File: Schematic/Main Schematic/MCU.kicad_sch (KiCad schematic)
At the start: 10 parts, among them J7 Conn_01x02_Pin, U4 M24C16-RMN6TP

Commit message: No change
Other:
- note removed: "TO-DO - Female headers should be inside MCU - UART Tx - Rx and Rx to Tx - Add Pull-up Resistors to SCL & SDA - Vcc connects to power not GND"
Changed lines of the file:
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@@
     (stroke (width 0) (type default))
-  )
-  (text "TO-DO\n- Female headers should be inside MCU\n- UART Tx - Rx and Rx to Tx\n- Add Pull-up Resistors to SCL & SDA\n- Vcc connects to power not GND\n"
-    (at 31.75 127 0)
-    (effects (font (size 1.27 1.27)) (justify left bottom))
   )
   (text "TEAM 26\nSIVUYILE NOSE\nMODULE INTERFACES WITH SENSOR AND POWER MODULES\nUCT\n"

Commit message: I've added the local footprints and gerber files into the repo
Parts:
- C8, C?: footprint A_New_folder:C1206 -> Local_Footprints:C1206
- U4: footprint A_New_folder:SOIC-8_L5.0-W4.0-P1.27-LS6.0-BL -> Local_Footprints:SOIC-8_L5.0-W4.0-P1.27-LS6.0-BL
- U?: footprint A_New_folder:SOP-16_L10.0-W3.9-P1.27-LS6.0-BL -> Local_Footprints:SOP-16_L10.0-W3.9-P1.27-LS6.0-BL
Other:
- note added: "TO-DO - Female headers should be inside MCU - UART Tx - Rx and Rx to Tx - Add Pull-up Resistors to SCL & SDA - Vcc connects to power not GND"
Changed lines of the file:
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@@
     (stroke (width 0) (type default))
+  )
+  (text "TO-DO\n- Female headers should be inside MCU\n- UART Tx - Rx and Rx to Tx\n- Add Pull-up Resistors to SCL & SDA\n- Vcc connects to power not GND\n"
+    (at 31.75 127 0)
+    (effects (font (size 1.27 1.27)) (justify left bottom))
   )
   (text "TEAM 26\nSIVUYILE NOSE\nMODULE INTERFACES WITH SENSOR AND POWER MODULES\nUCT\n"
@@
       (effects (font (size 1.27 1.27)))
     )
-    (property "Footprint" "A_New_folder:C1206" (at 107.95 40.9448 0)
+    (property "Footprint" "Local_Footprints:C1206" (at 107.95 40.9448 0)
       (effects (font (size 1.27 1.27)) hide)
     )
@@
       (effects (font (size 1.27 1.27)))
     )
-    (property "Footprint" "A_New_folder:SOP-16_L10.0-W3.9-P1.27-LS6.0-BL" (at 78.74 59.69 0)
+    (property "Footprint" "Local_Footprints:SOP-16_L10.0-W3.9-P1.27-LS6.0-BL" (at 78.74 59.69 0)
       (effects (font (size 1.27 1.27)) (justify bottom) hide)
     )
@@
       (effects (font (size 1.27 1.27)) (justify left))
     )
-    (property "Footprint" "A_New_folder:C1206" (at 251.1552 67.31 0)
+    (property "Footprint" "Local_Footprints:C1206" (at 251.1552 67.31 0)
       (effects (font (size 1.27 1.27)) hide)
     )
@@
       (effects (font (size 1.27 1.27)))
     )
-    (property "Footprint" "A_New_folder:SOIC-8_L5.0-W4.0-P1.27-LS6.0-BL" (at 215.9 64.77 0)
+    (property "Footprint" "Local_Footprints:SOIC-8_L5.0-W4.0-P1.27-LS6.0-BL" (at 215.9 64.77 0)
       (effects (font (size 1.27 1.27)) (justify left bottom) hide)
     )

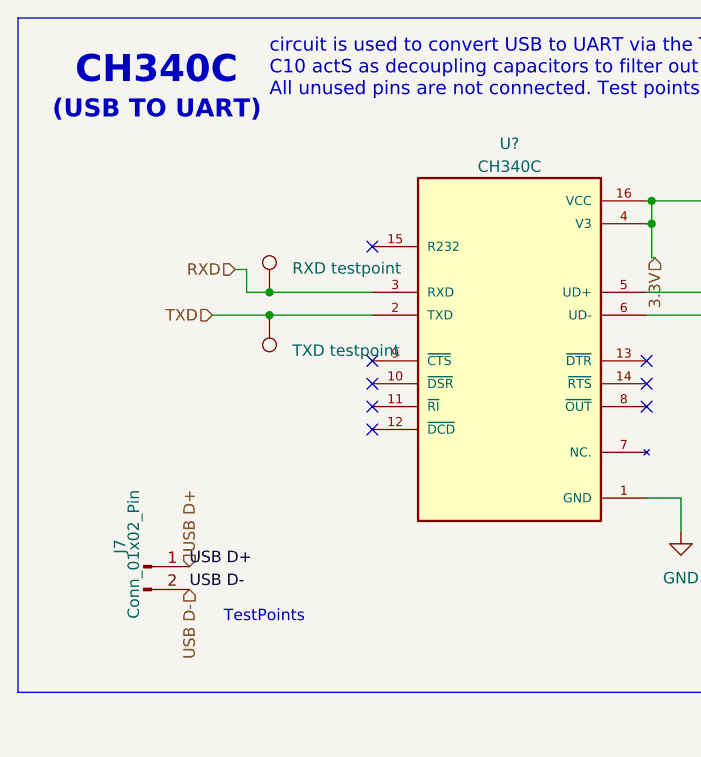
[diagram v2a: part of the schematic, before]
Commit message: LED added for visuals
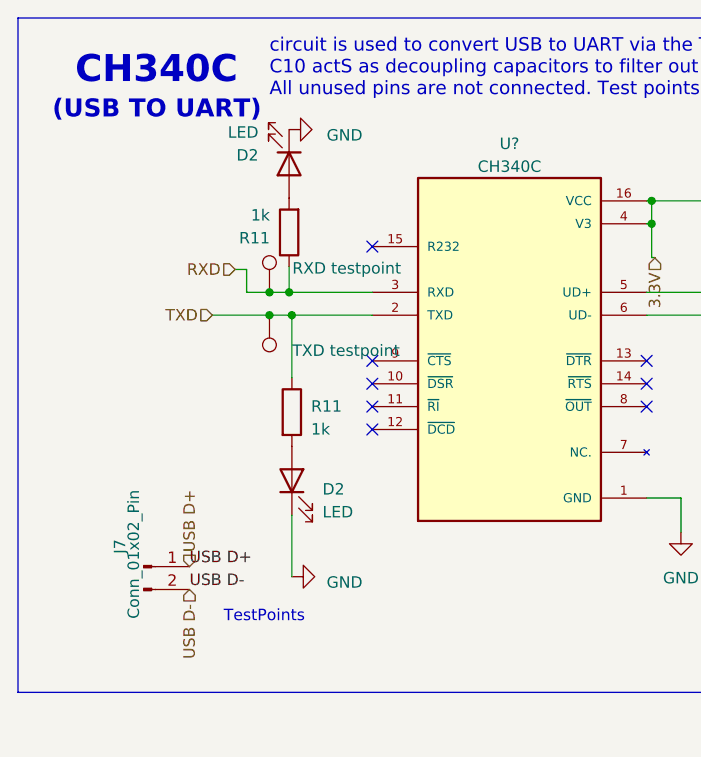
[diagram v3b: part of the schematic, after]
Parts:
- added D2 (x2): LED, symbol Device:LED
- added R11 (x2): 1k, symbol Device:R
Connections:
- net GND: now also D2.1 (K), D2.1 (K)
- net RXD: now also R11.1
- net TXD: now also R11.1
- new net: D2.2 (A), R11.2 (x2)
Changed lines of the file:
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@@
   (junction (at 191.77 57.15) (diameter 0) (color 0 0 0 0)
   )
+  (junction (at 54.5592 54.61) (diameter 0) (color 0 0 0 0)
+  )
   (junction (at 186.69 67.31) (diameter 0) (color 0 0 0 0)
   )
@@
   )
   (junction (at 52.07 52.07) (diameter 0) (color 0 0 0 0)
+  )
+  (junction (at 54.2544 52.07) (diameter 0) (color 0 0 0 0)
   )
   (junction (at 241.3 59.69) (diameter 0) (color 0 0 0 0)
@@
     (stroke (width 0) (type default))
   )
-  (wire (pts (xy 52.07 54.61) (xy 63.5 54.61))
+  (wire (pts (xy 52.07 54.61) (xy 54.5592 54.61))
     (stroke (width 0) (type default))
   )
@@
     (stroke (width 0) (type default))
   )
+  (wire (pts (xy 54.5592 54.61) (xy 54.5592 61.5696))
+    (stroke (width 0) (type default))
+  )
   (wire (pts (xy 194.31 69.85) (xy 200.66 69.85))
     (stroke (width 0) (type default))
@@
     (stroke (width 0) (type default))
   )
+  (wire (pts (xy 54.5592 54.61) (xy 63.5 54.61))
+    (stroke (width 0) (type default))
+  )
+  (wire (pts (xy 54.2544 49.2252) (xy 54.2544 52.07))
+    (stroke (width 0) (type default))
+  )
+  (wire (pts (xy 54.5592 76.8096) (xy 54.5592 83.6676))
+    (stroke (width 0) (type default))
+  )
   (wire (pts (xy 48.26 49.53) (xy 49.53 49.53))
     (stroke (width 0) (type default))
@@
     (stroke (width 0) (type default))
   )
+  (wire (pts (xy 54.2544 52.07) (xy 63.5 52.07))
+    (stroke (width 0) (type default))
+  )
   (wire (pts (xy 200.66 62.23) (xy 186.69 62.23))
     (stroke (width 0) (type default))
@@
     (stroke (width 0) (type default))
   )
-  (wire (pts (xy 52.07 52.07) (xy 63.5 52.07))
+  (wire (pts (xy 52.07 52.07) (xy 54.2544 52.07))
     (stroke (width 0) (type default))
   )
@@
     )
   )
+  (symbol (lib_id "Device:R") (at 54.2544 45.4152 180) (unit 1)
+    (in_bom yes) (on_board yes) (dnp no) (fields_autoplaced)
+    (property "Reference" "R11" (at 52.1208 46.0502 0)
+      (effects (font (size 1.27 1.27)) (justify left))
+    )
+    (property "Value" "1k" (at 52.1208 43.5102 0)
+      (effects (font (size 1.27 1.27)) (justify left))
+    )
+    (property "Footprint" "" (at 56.0324 45.4152 90)
+      (effects (font (size 1.27 1.27)) hide)
+    )
+    (property "Datasheet" "~" (at 54.2544 45.4152 0)
+      (effects (font (size 1.27 1.27)) hide)
+    )
+    (pin "1")
+    (pin "2")
+    (instances
+      (project "Main Schematic"
+        (path "/81c41bad-bb43-41af-b405-18d135a809b1/297def35-fe1a-4185-9e34-6248c2c818f7"
+          (reference "R11") (unit 1)
+        )
+        (path "/81c41bad-bb43-41af-b405-18d135a809b1/ae15d31d-f7b4-4051-b9d0-3a01939afe0e"
+          (reference "R15") (unit 1)
+        )
+      )
+    )
+  )
   (symbol (lib_id "power:GND") (at 186.69 68.58 0) (unit 1)
     (in_bom yes) (on_board yes) (dnp no) (fields_autoplaced)
@@
     )
   )
+  (symbol (lib_id "power:GND") (at 54.2544 33.9852 90) (unit 1)
+    (in_bom yes) (on_board yes) (dnp no) (fields_autoplaced)
+    (property "Reference" "#PWR024" (at 60.6044 33.9852 0)
+      (effects (font (size 1.27 1.27)) hide)
+    )
+    (property "Value" "GND" (at 58.42 34.6202 90)
+      (effects (font (size 1.27 1.27)) (justify right))
+    )
+    (property "Footprint" "" (at 54.2544 33.9852 0)
+      (effects (font (size 1.27 1.27)) hide)
+    )
+    (property "Datasheet" "" (at 54.2544 33.9852 0)
+      (effects (font (size 1.27 1.27)) hide)
+    )
+    (pin "1")
+    (instances
+      (project "Main Schematic"
+        (path "/81c41bad-bb43-41af-b405-18d135a809b1/ae15d31d-f7b4-4051-b9d0-3a01939afe0e"
+          (reference "#PWR024") (unit 1)
+        )
+      )
+    )
+  )
+  (symbol (lib_id "power:GND") (at 54.5592 83.6676 90) (unit 1)
+    (in_bom yes) (on_board yes) (dnp no) (fields_autoplaced)
+    (property "Reference" "#PWR07" (at 60.9092 83.6676 0)
+      (effects (font (size 1.27 1.27)) hide)
+    )
+    (property "Value" "GND" (at 58.42 84.3026 90)
+      (effects (font (size 1.27 1.27)) (justify right))
+    )
+    (property "Footprint" "" (at 54.5592 83.6676 0)
+      (effects (font (size 1.27 1.27)) hide)
+    )
+    (property "Datasheet" "" (at 54.5592 83.6676 0)
+      (effects (font (size 1.27 1.27)) hide)
+    )
+    (pin "1")
+    (instances
+      (project "Main Schematic"
+        (path "/81c41bad-bb43-41af-b405-18d135a809b1/ae15d31d-f7b4-4051-b9d0-3a01939afe0e"
+          (reference "#PWR07") (unit 1)
+        )
+      )
+    )
+  )
   (symbol (lib_id "Connector:TestPoint") (at 52.07 54.61 180) (unit 1)
     (in_bom yes) (on_board yes) (dnp no) (fields_autoplaced)
@@
     )
   )
+  (symbol (lib_id "Device:LED") (at 54.2544 37.7952 270) (unit 1)
+    (in_bom yes) (on_board yes) (dnp no) (fields_autoplaced)
+    (property "Reference" "D2" (at 50.8508 36.8427 90)
+      (effects (font (size 1.27 1.27)) (justify right))
+    )
+    (property "Value" "LED" (at 50.8508 34.3027 90)
+      (effects (font (size 1.27 1.27)) (justify right))
+    )
+    (property "Footprint" "" (at 54.2544 37.7952 0)
+      (effects (font (size 1.27 1.27)) hide)
+    )
+    (property "Datasheet" "~" (at 54.2544 37.7952 0)
+      (effects (font (size 1.27 1.27)) hide)
+    )
+    (pin "1")
+    (pin "2")
+    (instances
+      (project "Main Schematic"
+        (path "/81c41bad-bb43-41af-b405-18d135a809b1/297def35-fe1a-4185-9e34-6248c2c818f7"
+          (reference "D2") (unit 1)
+        )
+        (path "/81c41bad-bb43-41af-b405-18d135a809b1/ae15d31d-f7b4-4051-b9d0-3a01939afe0e"
+          (reference "D6") (unit 1)
+        )
+      )
+    )
+  )
+  (symbol (lib_id "Device:LED") (at 54.5592 72.9996 90) (unit 1)
+    (in_bom yes) (on_board yes) (dnp no) (fields_autoplaced)
+    (property "Reference" "D2" (at 57.9628 73.9521 90)
+      (effects (font (size 1.27 1.27)) (justify right))
+    )
+    (property "Value" "LED" (at 57.9628 76.4921 90)
+      (effects (font (size 1.27 1.27)) (justify right))
+    )
+    (property "Footprint" "" (at 54.5592 72.9996 0)
+      (effects (font (size 1.27 1.27)) hide)
+    )
+    (property "Datasheet" "~" (at 54.5592 72.9996 0)
+      (effects (font (size 1.27 1.27)) hide)
+    )
+    (pin "1")
+    (pin "2")
+    (instances
+      (project "Main Schematic"
+        (path "/81c41bad-bb43-41af-b405-18d135a809b1/297def35-fe1a-4185-9e34-6248c2c818f7"
+          (reference "D2") (unit 1)
+        )
+        (path "/81c41bad-bb43-41af-b405-18d135a809b1/ae15d31d-f7b4-4051-b9d0-3a01939afe0e"
+          (reference "D5") (unit 1)
+        )
+      )
+    )
+  )
   (symbol (lib_id "Connector:TestPoint") (at 234.95 64.77 270) (unit 1)
     (in_bom yes) (on_board yes) (dnp no) (fields_autoplaced)
@@
         )
       )
+    )
+  )
+  (symbol (lib_id "Device:R") (at 54.5592 65.3796 0) (unit 1)
+    (in_bom yes) (on_board yes) (dnp no) (fields_autoplaced)
+    (property "Reference" "R11" (at 56.6928 64.7446 0)
+      (effects (font (size 1.27 1.27)) (justify left))
+    )
+    (property "Value" "1k" (at 56.6928 67.2846 0)
+      (effects (font (size 1.27 1.27)) (justify left))
+    )
+    (property "Footprint" "" (at 52.7812 65.3796 90)
+      (effects (font (size 1.27 1.27)) hide)
+    )
+    (property "Datasheet" "~" (at 54.5592 65.3796 0)
+      (effects (font (size 1.27 1.27)) hide)
+    )
+    (pin "1")
+    (pin "2")
+    (instances
+      (project "Main Schematic"
+        (path "/81c41bad-bb43-41af-b405-18d135a809b1/297def35-fe1a-4185-9e34-6248c2c818f7"
+          (reference "R11") (unit 1)
+        )
+        (path "/81c41bad-bb43-41af-b405-18d135a809b1/ae15d31d-f7b4-4051-b9d0-3a01939afe0e"
+          (reference "R14") (unit 1)
+        )
+      )

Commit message: Added more led for visual indications, also changed debugger pins to 9 pins for 3.3v pin
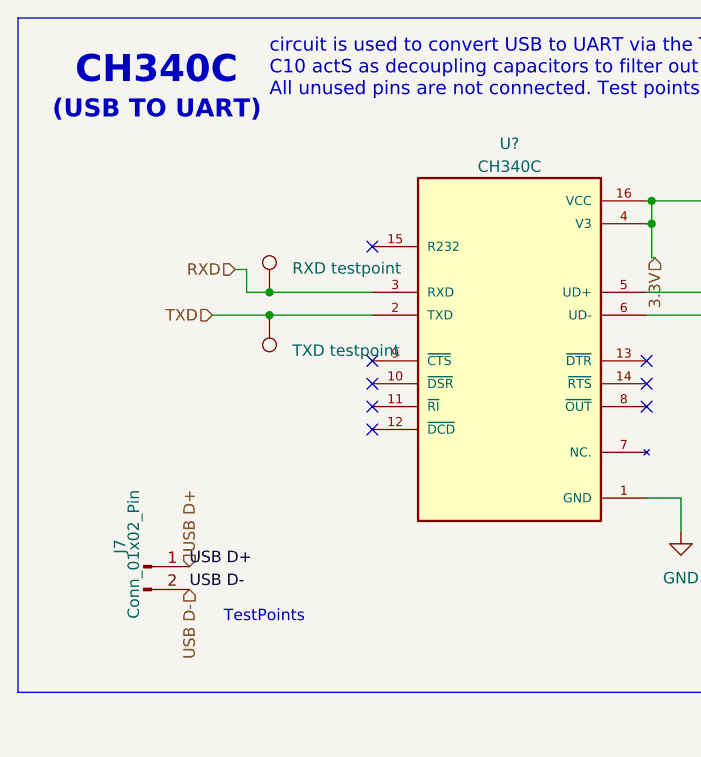
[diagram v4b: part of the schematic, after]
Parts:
- removed D2 (x2): LED, symbol Device:LED
- removed R11 (x2): 1k, symbol Device:R
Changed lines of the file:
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@@
   (junction (at 191.77 57.15) (diameter 0) (color 0 0 0 0)
   )
-  (junction (at 54.5592 54.61) (diameter 0) (color 0 0 0 0)
-  )
   (junction (at 186.69 67.31) (diameter 0) (color 0 0 0 0)
   )
@@
   )
   (junction (at 52.07 52.07) (diameter 0) (color 0 0 0 0)
-  )
-  (junction (at 54.2544 52.07) (diameter 0) (color 0 0 0 0)
   )
   (junction (at 241.3 59.69) (diameter 0) (color 0 0 0 0)
@@
     (stroke (width 0) (type default))
   )
-  (wire (pts (xy 52.07 54.61) (xy 54.5592 54.61))
-    (stroke (width 0) (type default))
-  )
   (wire (pts (xy 94.5388 41.91) (xy 100.33 41.91))
     (stroke (width 0) (type default))
@@
     (stroke (width 0) (type default))
   )
-  (wire (pts (xy 54.5592 54.61) (xy 54.5592 61.5696))
-    (stroke (width 0) (type default))
-  )
   (wire (pts (xy 194.31 69.85) (xy 200.66 69.85))
     (stroke (width 0) (type default))
@@
     (stroke (width 0) (type default))
   )
-  (wire (pts (xy 54.5592 54.61) (xy 63.5 54.61))
-    (stroke (width 0) (type default))
-  )
-  (wire (pts (xy 54.2544 49.2252) (xy 54.2544 52.07))
-    (stroke (width 0) (type default))
-  )
-  (wire (pts (xy 54.5592 76.8096) (xy 54.5592 83.6676))
+  (wire (pts (xy 52.07 54.61) (xy 63.5 54.61))
     (stroke (width 0) (type default))
   )
@@
     (stroke (width 0) (type default))
   )
-  (wire (pts (xy 54.2544 52.07) (xy 63.5 52.07))
-    (stroke (width 0) (type default))
-  )
   (wire (pts (xy 200.66 62.23) (xy 186.69 62.23))
     (stroke (width 0) (type default))
@@
     (stroke (width 0) (type default))
   )
-  (wire (pts (xy 52.07 52.07) (xy 54.2544 52.07))
+  (wire (pts (xy 52.07 52.07) (xy 63.5 52.07))
     (stroke (width 0) (type default))
   )
@@
     )
   )
-  (symbol (lib_id "Device:R") (at 54.2544 45.4152 180) (unit 1)
-    (in_bom yes) (on_board yes) (dnp no) (fields_autoplaced)
-    (property "Reference" "R11" (at 52.1208 46.0502 0)
-      (effects (font (size 1.27 1.27)) (justify left))
-    )
-    (property "Value" "1k" (at 52.1208 43.5102 0)
-      (effects (font (size 1.27 1.27)) (justify left))
-    )
-    (property "Footprint" "" (at 56.0324 45.4152 90)
-      (effects (font (size 1.27 1.27)) hide)
-    )
-    (property "Datasheet" "~" (at 54.2544 45.4152 0)
-      (effects (font (size 1.27 1.27)) hide)
-    )
-    (pin "1")
-    (pin "2")
-    (instances
-      (project "Main Schematic"
-        (path "/81c41bad-bb43-41af-b405-18d135a809b1/297def35-fe1a-4185-9e34-6248c2c818f7"
-          (reference "R11") (unit 1)
-        )
-        (path "/81c41bad-bb43-41af-b405-18d135a809b1/ae15d31d-f7b4-4051-b9d0-3a01939afe0e"
-          (reference "R15") (unit 1)
-        )
-      )
-    )
-  )
   (symbol (lib_id "power:GND") (at 186.69 68.58 0) (unit 1)
     (in_bom yes) (on_board yes) (dnp no) (fields_autoplaced)
@@
     )
   )
-  (symbol (lib_id "power:GND") (at 54.2544 33.9852 90) (unit 1)
-    (in_bom yes) (on_board yes) (dnp no) (fields_autoplaced)
-    (property "Reference" "#PWR024" (at 60.6044 33.9852 0)
-      (effects (font (size 1.27 1.27)) hide)
-    )
-    (property "Value" "GND" (at 58.42 34.6202 90)
-      (effects (font (size 1.27 1.27)) (justify right))
-    )
-    (property "Footprint" "" (at 54.2544 33.9852 0)
-      (effects (font (size 1.27 1.27)) hide)
-    )
-    (property "Datasheet" "" (at 54.2544 33.9852 0)
-      (effects (font (size 1.27 1.27)) hide)
-    )
-    (pin "1")
-    (instances
-      (project "Main Schematic"
-        (path "/81c41bad-bb43-41af-b405-18d135a809b1/ae15d31d-f7b4-4051-b9d0-3a01939afe0e"
-          (reference "#PWR024") (unit 1)
-        )
-      )
-    )
-  )
-  (symbol (lib_id "power:GND") (at 54.5592 83.6676 90) (unit 1)
-    (in_bom yes) (on_board yes) (dnp no) (fields_autoplaced)
-    (property "Reference" "#PWR07" (at 60.9092 83.6676 0)
-      (effects (font (size 1.27 1.27)) hide)
-    )
-    (property "Value" "GND" (at 58.42 84.3026 90)
-      (effects (font (size 1.27 1.27)) (justify right))
-    )
-    (property "Footprint" "" (at 54.5592 83.6676 0)
-      (effects (font (size 1.27 1.27)) hide)
-    )
-    (property "Datasheet" "" (at 54.5592 83.6676 0)
-      (effects (font (size 1.27 1.27)) hide)
-    )
-    (pin "1")
-    (instances
-      (project "Main Schematic"
-        (path "/81c41bad-bb43-41af-b405-18d135a809b1/ae15d31d-f7b4-4051-b9d0-3a01939afe0e"
-          (reference "#PWR07") (unit 1)
-        )
-      )
-    )
-  )
   (symbol (lib_id "Connector:TestPoint") (at 52.07 54.61 180) (unit 1)
     (in_bom yes) (on_board yes) (dnp no) (fields_autoplaced)
@@
         (path "/e63e39d7-6ac0-4ffd-8aa3-1841a4541b55/59b42903-2dc7-4011-ab5b-d7b81bd233c3"
           (reference "TP?") (unit 1)
-        )
-      )
-    )
-  )
-  (symbol (lib_id "Device:LED") (at 54.2544 37.7952 270) (unit 1)
-    (in_bom yes) (on_board yes) (dnp no) (fields_autoplaced)
-    (property "Reference" "D2" (at 50.8508 36.8427 90)
-      (effects (font (size 1.27 1.27)) (justify right))
-    )
-    (property "Value" "LED" (at 50.8508 34.3027 90)
-      (effects (font (size 1.27 1.27)) (justify right))
-    )
-    (property "Footprint" "" (at 54.2544 37.7952 0)
-      (effects (font (size 1.27 1.27)) hide)
-    )
-    (property "Datasheet" "~" (at 54.2544 37.7952 0)
-      (effects (font (size 1.27 1.27)) hide)
-    )
-    (pin "1")
-    (pin "2")
-    (instances
-      (project "Main Schematic"
-        (path "/81c41bad-bb43-41af-b405-18d135a809b1/297def35-fe1a-4185-9e34-6248c2c818f7"
-          (reference "D2") (unit 1)
-        )
-        (path "/81c41bad-bb43-41af-b405-18d135a809b1/ae15d31d-f7b4-4051-b9d0-3a01939afe0e"
-          (reference "D6") (unit 1)
-        )
-      )
-    )
-  )
-  (symbol (lib_id "Device:LED") (at 54.5592 72.9996 90) (unit 1)
-    (in_bom yes) (on_board yes) (dnp no) (fields_autoplaced)
-    (property "Reference" "D2" (at 57.9628 73.9521 90)
-      (effects (font (size 1.27 1.27)) (justify right))
-    )
-    (property "Value" "LED" (at 57.9628 76.4921 90)
-      (effects (font (size 1.27 1.27)) (justify right))
-    )
-    (property "Footprint" "" (at 54.5592 72.9996 0)
-      (effects (font (size 1.27 1.27)) hide)
-    )
-    (property "Datasheet" "~" (at 54.5592 72.9996 0)
-      (effects (font (size 1.27 1.27)) hide)
-    )
-    (pin "1")
-    (pin "2")
-    (instances
-      (project "Main Schematic"
-        (path "/81c41bad-bb43-41af-b405-18d135a809b1/297def35-fe1a-4185-9e34-6248c2c818f7"
-          (reference "D2") (unit 1)
-        )
-        (path "/81c41bad-bb43-41af-b405-18d135a809b1/ae15d31d-f7b4-4051-b9d0-3a01939afe0e"
-          (reference "D5") (unit 1)
         )
       )
@@
         )
       )
-    )
-  )
-  (symbol (lib_id "Device:R") (at 54.5592 65.3796 0) (unit 1)
-    (in_bom yes) (on_board yes) (dnp no) (fields_autoplaced)
-    (property "Reference" "R11" (at 56.6928 64.7446 0)
-      (effects (font (size 1.27 1.27)) (justify left))
-    )
-    (property "Value" "1k" (at 56.6928 67.2846 0)
-      (effects (font (size 1.27 1.27)) (justify left))
-    )
-    (property "Footprint" "" (at 52.7812 65.3796 90)
-      (effects (font (size 1.27 1.27)) hide)
-    )
-    (property "Datasheet" "~" (at 54.5592 65.3796 0)
-      (effects (font (size 1.27 1.27)) hide)
-    )
-    (pin "1")
-    (pin "2")
-    (instances
-      (project "Main Schematic"
-        (path "/81c41bad-bb43-41af-b405-18d135a809b1/297def35-fe1a-4185-9e34-6248c2c818f7"
-          (reference "R11") (unit 1)
-        )
-        (path "/81c41bad-bb43-41af-b405-18d135a809b1/ae15d31d-f7b4-4051-b9d0-3a01939afe0e"
-          (reference "R14") (unit 1)
-        )
-      )
